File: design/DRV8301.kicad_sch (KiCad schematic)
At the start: 38 parts, among them U2 LM3671, U3 DRV8301

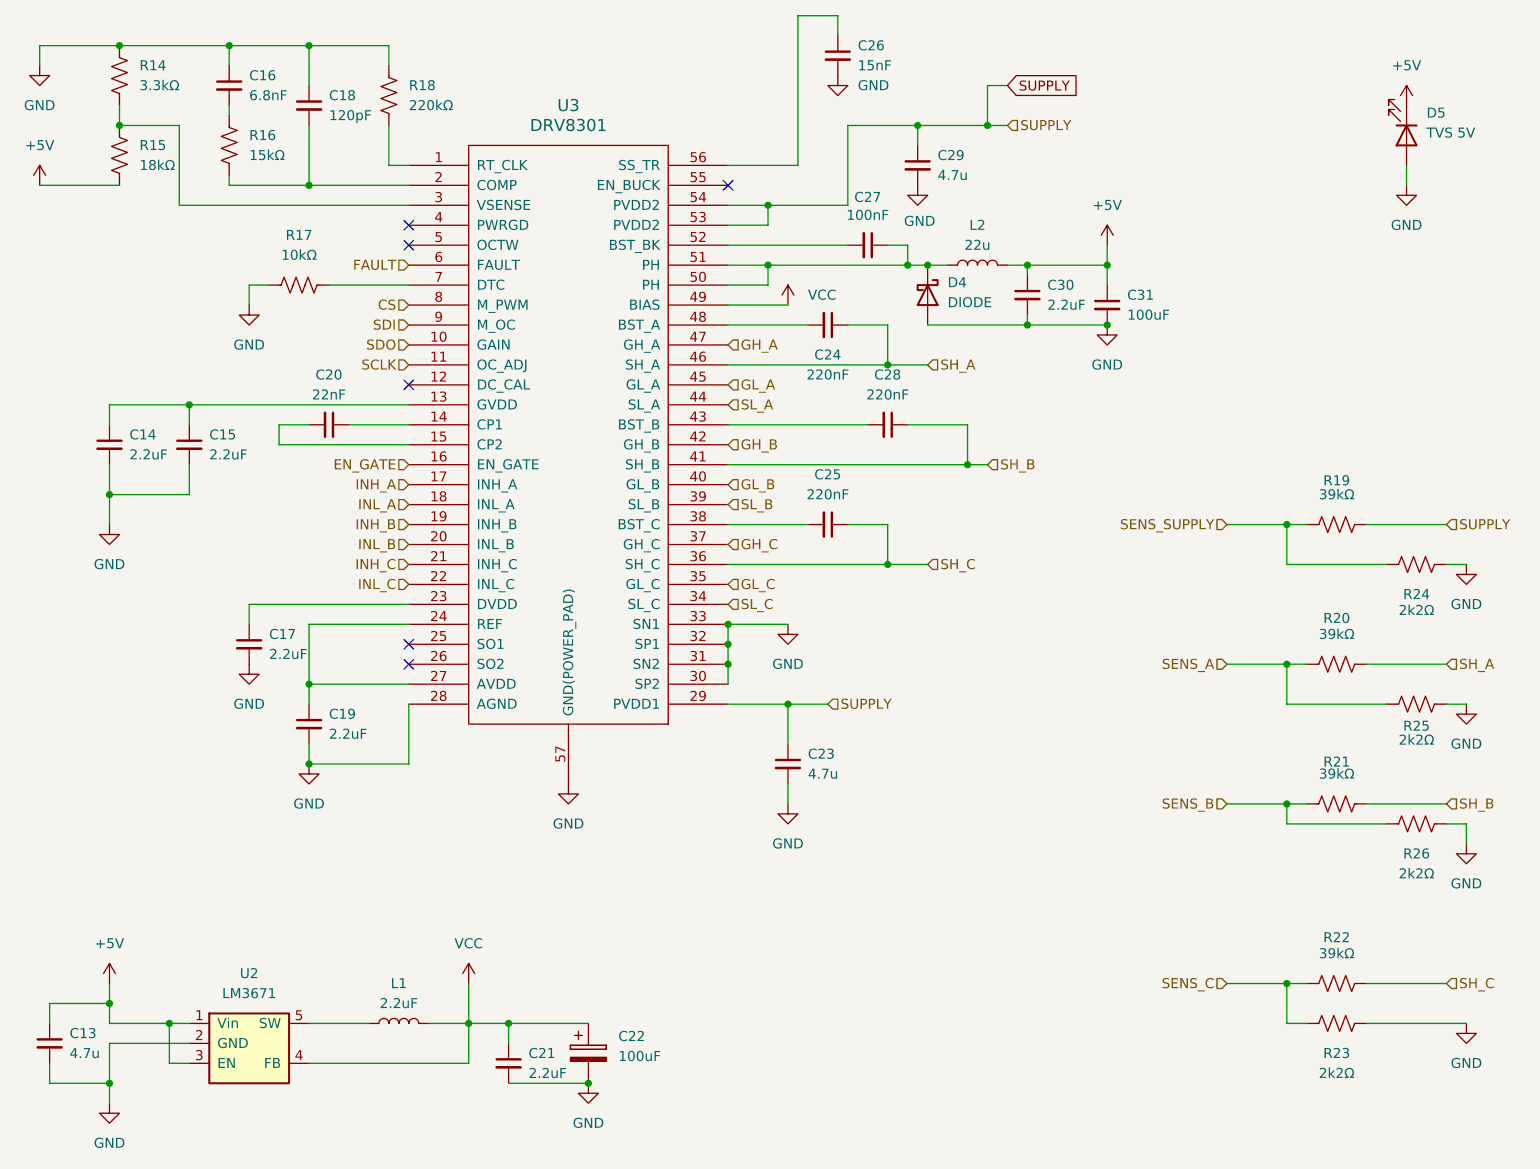
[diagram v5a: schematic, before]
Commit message: Ordenado del esquemático
- Cambios en los capacitores del oscilador
- Mejora de los esquemáticos, encapsulado la interfáz usb y los sensores del motor
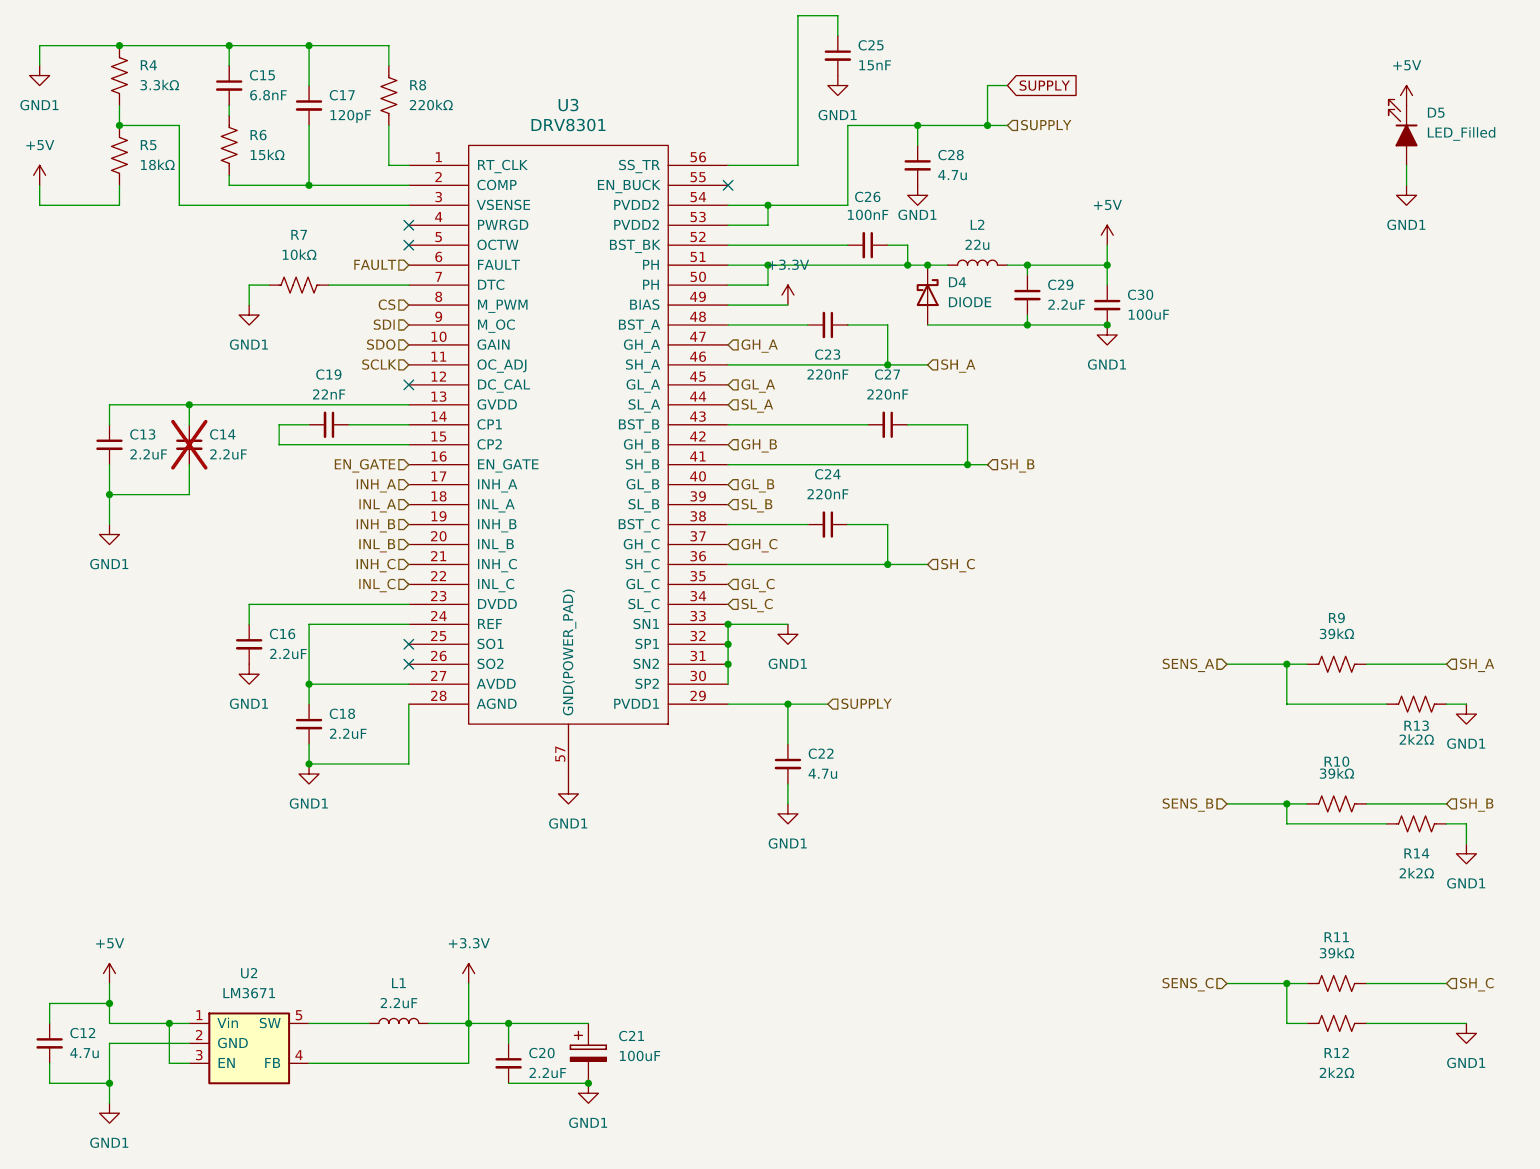
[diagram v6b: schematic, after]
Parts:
- removed R19: 39kΩ, Resistor_SMD:R_0603_1608Metric, symbol Device:R_US
- removed R24: 2k2Ω, Resistor_SMD:R_0603_1608Metric, symbol Device:R_US
- C14: renamed from C15; now not fitted; now left out of the parts list
- D5: value TVS 5V -> LED_Filled; symbol Device:LED -> Device:LED_Filled
- renumbered C13 to C12, C14 to C13, C16 to C15, C17 to C16, C18 to C17, C19 to C18, C20 to C19, C21 to C20, C22 to C21, C23 to C22, C24 to C23, C25 to C24, C26 to C25, C27 to C26, C28 to C27, C29 to C28, C30 to C29, C31 to C30, R21 to R10, R22 to R11, R23 to R12, R25 to R13, R26 to R14, R14 to R4, R15 to R5, R16 to R6, R17 to R7, R18 to R8, R20 to R9
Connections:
- net GND renamed GND1
- net VCC renamed +3.3V

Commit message: Pequeños cambios
Pequeños cambios, eliminado de carpeta BLDC
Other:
- moved on the sheet: C20
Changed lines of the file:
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@@
 	(wire
 		(pts
-			(xy 134.62 147.32) (xy 134.62 149.86)
+			(xy 134.62 147.32) (xy 134.62 148.59)
 		)
 		(stroke
@@
 	(wire
 		(pts
+			(xy 134.62 154.94) (xy 134.62 153.67)
+		)
+		(stroke
+			(width 0)
+			(type default)
+		)
+	)
+	(wire
+		(pts
 			(xy 177.8 43.18) (xy 177.8 33.02)
 		)
@@
 	(symbol
 		(lib_id "Device:C_Small")
-		(at 134.62 152.4 0)
+		(at 134.62 151.13 0)
 		(unit 1)
 		(exclude_from_sim no)
@@
 		(fields_autoplaced yes)
 		(property "Reference" "C20"
-			(at 137.16 151.1362 0)
+			(at 137.16 149.8662 0)
 			(effects
 				(font
@@
 		)
 		(property "Value" "2.2uF"
-			(at 137.16 153.6762 0)
+			(at 137.16 152.4062 0)
 			(effects
 				(font
@@
 		)
 		(property "Footprint" "Capacitor_SMD:C_0603_1608Metric"
-			(at 134.62 152.4 0)
+			(at 134.62 151.13 0)
 			(effects
 				(font
@@
 		)
 		(property "Datasheet" "~"
-			(at 134.62 152.4 0)
+			(at 134.62 151.13 0)
 			(effects
 				(font
@@
 		)
 		(property "Description" "CAP 2.2u, 16V, 0603"
-			(at 134.62 152.4 0)
+			(at 134.62 151.13 0)
 			(effects
 				(font
@@
 		)
 		(property "Manufacturer" "Samsung Electro-Mechanics"
-			(at 134.62 152.4 0)
+			(at 134.62 151.13 0)
 			(effects
 				(font
@@
 		)
 		(property "Manufacturer Product Number " "CL10A225KO8NNNC"
-			(at 134.62 152.4 0)
+			(at 134.62 151.13 0)
 			(effects
 				(font
@@
 		)
 		(property "Availability" ""
-			(at 134.62 152.4 0)
+			(at 134.62 151.13 0)
 			(effects
 				(font
@@
 		)
 		(property "Check_prices" ""
-			(at 134.62 152.4 0)
+			(at 134.62 151.13 0)
 			(effects
 				(font
@@
 		)
 		(property "Description_1" ""
-			(at 134.62 152.4 0)
+			(at 134.62 151.13 0)
 			(effects
 				(font
@@
 		)
 		(property "MANUFACTURER" ""
-			(at 134.62 152.4 0)
+			(at 134.62 151.13 0)
 			(effects
 				(font
@@
 		)
 		(property "MF" ""
-			(at 134.62 152.4 0)
+			(at 134.62 151.13 0)
 			(effects
 				(font
@@
 		)
 		(property "MP" ""
-			(at 134.62 152.4 0)
+			(at 134.62 151.13 0)
 			(effects
 				(font
@@
 		)
 		(property "Package" ""
-			(at 134.62 152.4 0)
+			(at 134.62 151.13 0)
 			(effects
 				(font
@@
 		)
 		(property "Price" ""
-			(at 134.62 152.4 0)
+			(at 134.62 151.13 0)
 			(effects
 				(font
@@
 		)
 		(property "Purchase-URL" ""
-			(at 134.62 152.4 0)
+			(at 134.62 151.13 0)
 			(effects
 				(font
@@
 		)
 		(property "STANDARD" ""
-			(at 134.62 152.4 0)
+			(at 134.62 151.13 0)
 			(effects
 				(font
@@
 		)
 		(property "SnapEDA_Link" ""
-			(at 134.62 152.4 0)
+			(at 134.62 151.13 0)
 			(effects
 				(font

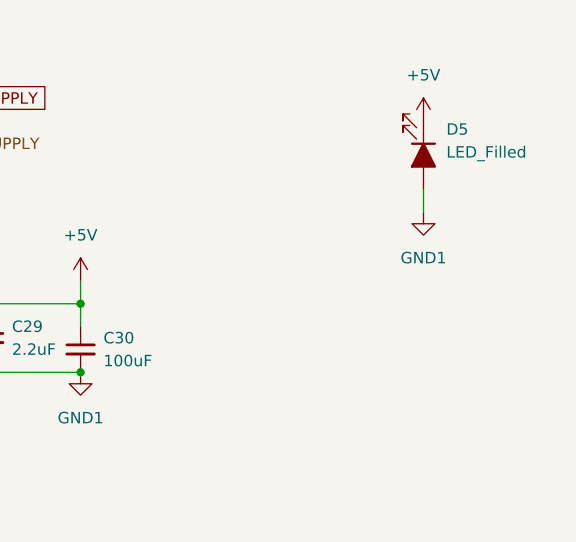
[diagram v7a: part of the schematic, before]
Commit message: Complete ruteo, menos plano GND2
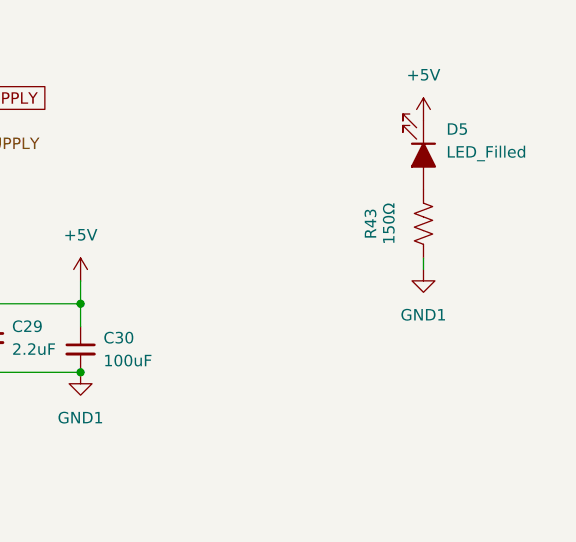
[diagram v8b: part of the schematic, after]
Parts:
- added R43: 150Ω, Resistor_SMD:R_0603_1608Metric, symbol Device:R_US
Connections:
- net GND1: now also R43.2; no longer D5.2 (A)
- new net: D5.2 (A), R43.1
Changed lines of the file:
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@@
 	(wire
 		(pts
-			(xy 248.92 38.1) (xy 248.92 40.64)
-		)
-		(stroke
-			(width 0)
-			(type default)
-		)
-	)
-	(wire
-		(pts
 			(xy 91.44 147.32) (xy 93.98 147.32)
 		)
@@
 	(wire
 		(pts
+			(xy 248.92 45.72) (xy 248.92 46.99)
+		)
+		(stroke
+			(width 0)
+			(type default)
+		)
+	)
+	(wire
+		(pts
 			(xy 109.22 22.86) (xy 109.22 27.94)
 		)
@@
 	(symbol
 		(lib_id "power:GND1")
-		(at 248.92 40.64 0)
+		(at 248.92 46.99 0)
 		(unit 1)
 		(exclude_from_sim no)
@@
 		(fields_autoplaced yes)
 		(property "Reference" "#PWR035"
-			(at 248.92 46.99 0)
+			(at 248.92 53.34 0)
 			(effects
 				(font
@@
 		)
 		(property "Value" "GND1"
-			(at 248.92 45.72 0)
+			(at 248.92 52.07 0)
 			(effects
 				(font
@@
 		)
 		(property "Footprint" ""
-			(at 248.92 40.64 0)
+			(at 248.92 46.99 0)
 			(effects
 				(font
@@
 		)
 		(property "Datasheet" ""
-			(at 248.92 40.64 0)
+			(at 248.92 46.99 0)
 			(effects
 				(font
@@
 		)
 		(property "Description" "Power symbol creates a global label with name \"GND1\" , ground"
-			(at 248.92 40.64 0)
+			(at 248.92 46.99 0)
 			(effects
 				(font
@@
 					(unit 1)
 				)
+			)
+		)
+	)
+	(symbol
+		(lib_id "Device:R_US")
+		(at 248.92 41.91 0)
+		(unit 1)
+		(exclude_from_sim no)
+		(in_bom yes)
+		(on_board yes)
+		(dnp no)
+		(property "Reference" "R43"
+			(at 243.078 41.91 90)
+			(effects
+				(font
+					(size 1.27 1.27)
+				)
+			)
+		)
+		(property "Value" "150Ω"
+			(at 245.11 41.91 90)
+			(effects
+				(font
+					(size 1.27 1.27)
+				)
+			)
+		)
+		(property "Footprint" "Resistor_SMD:R_0603_1608Metric"
+			(at 249.936 42.164 90)
+			(effects
+				(font
+					(size 1.27 1.27)
+				)
+				(hide yes)
+			)
+		)
+		(property "Datasheet" "~"
+			(at 248.92 41.91 0)
+			(effects
+				(font
+					(size 1.27 1.27)
+				)
+				(hide yes)
+			)
+		)
+		(property "Description" ""
+			(at 248.92 41.91 0)
+			(effects
+				(font
+					(size 1.27 1.27)
+				)
+				(hide yes)
+			)
+		)
+		(property "Manufacturer" "CAL-CHIP ELECTRONICS, INC."
+			(at 248.92 41.91 0)
+			(effects
+				(font
+					(size 1.27 1.27)
+				)
+				(hide yes)
+			)
+		)
+		(property "Manufacturer Product Number " "RM06F1500CT"
+			(at 248.92 41.91 0)
+			(effects
+				(font
+					(size 1.27 1.27)
+				)
+				(hide yes)
+			)
+		)
+		(property "Availability" ""
+			(at 248.92 41.91 0)
+			(effects
+				(font
+					(size 1.27 1.27)
+				)
+				(hide yes)
+			)
+		)
+		(property "Check_prices" ""
+			(at 248.92 41.91 0)
+			(effects
+				(font
+					(size 1.27 1.27)
+				)
+				(hide yes)
+			)
+		)
+		(property "Description_1" ""
+			(at 248.92 41.91 0)
+			(effects
+				(font
+					(size 1.27 1.27)
+				)
+				(hide yes)
+			)
+		)
+		(property "MANUFACTURER" ""
+			(at 248.92 41.91 0)
+			(effects
+				(font
+					(size 1.27 1.27)
+				)
+				(hide yes)
+			)
+		)
+		(property "MF" ""
+			(at 248.92 41.91 0)
+			(effects
+				(font
+					(size 1.27 1.27)
+				)
+				(hide yes)
+			)
+		)
+		(property "MP" ""
+			(at 248.92 41.91 0)
+			(effects
+				(font
+					(size 1.27 1.27)
+				)
+				(hide yes)
+			)
+		)
+		(property "Package" ""
+			(at 248.92 41.91 0)
+			(effects
+				(font
+					(size 1.27 1.27)
+				)
+				(hide yes)
+			)
+		)
+		(property "Price" ""
+			(at 248.92 41.91 0)
+			(effects
+				(font
+					(size 1.27 1.27)
+				)
+				(hide yes)
+			)
+		)
+		(property "Purchase-URL" ""
+			(at 248.92 41.91 0)
+			(effects
+				(font
+					(size 1.27 1.27)
+				)
+				(hide yes)
+			)
+		)
+		(property "STANDARD" ""
+			(at 248.92 41.91 0)
+			(effects
+				(font
+					(size 1.27 1.27)
+				)
+				(hide yes)
+			)
+		)
+		(property "SnapEDA_Link" ""
+			(at 248.92 41.91 0)
+			(effects
+				(font
+					(size 1.27 1.27)
+				)
+				(hide yes)
+			)
+		)
+		(pin "1"
+		)
+		(pin "2"
+		)
+		(instances
+			(project "ESCX"
+				(path "/6389d757-a1bd-4c0a-9d55-6114b19cc67a/00000000-0000-0000-0000-00005ae1478f"
+					(reference "R43")
+					(unit 1)
+				)
